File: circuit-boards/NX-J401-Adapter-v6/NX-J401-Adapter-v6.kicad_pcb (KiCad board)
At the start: 2 copper layers, 120 x 79 mm, 146 parts, among them J1 NX BUTTON, J10 SWD, J11 CFG, J12 NX CONTROL & UART, J13 NX BUTTON, J14 USB_C_Receptacle_USB2.0_14P, J2 POWER, J3 USB1, J4 USB2, J5 CAN1, J6 CAN1, J7 15V, J8 SWD, J9 CFG, Q1 SQM120P06-07L_GE3, Q10 SS8050, Q11 SI2301CDS-T1-GE3, Q2 CSD19534Q5A, Q3 CSD19534Q5A, Q4 CSD17578Q5A, Q5 CSD17578Q5A, Q6 SI2301CDS-T1-GE3, Q7 SS8050, Q8 SI2301CDS-T1-GE3, Q9 SI2301CDS-T1-GE3, SW1 RECOVERY, SW2 RESET, U2 RT9013-33GB, U3 STM32G431CBTx, U4 TJA1051TK-3, U5 RT9013-33GB, U6 STM32G431CBTx, U7 TJA1051TK-3, U8 FT232RNL, U9 ISO6721BDR

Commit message: Changed canable to use 3.3V power form USB to use key-e connector that breaks out USB and 3V3
Signed-off-by: Scott Berman <sgberman1@gmail.com>
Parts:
- removed C35, C39, C50: 1uF-50V-10%-0603, Capacitor_SMD:C_0603_1608Metric
- removed C49, C51, C52, C53, C55, C56: 0.1uF-50V-10%-0603, Capacitor_SMD:C_0603_1608Metric
- removed C54: 22uF-10%-16V-0805, Capacitor_SMD:C_0805_2012Metric
- removed D1: PC, LED_THT:LED_D3.0mm_Horizontal_O1.27mm_Z2.0mm
- removed J10: SWD, Connector_PinHeader_2.54mm:PinHeader_1x04_P2.54mm_Vertical
- removed J11: CFG, Connector_PinHeader_2.54mm:PinHeader_2x02_P2.54mm_Vertical
- removed J4: USB2, NX-J401-Adapter:Molex-70555-0003
- removed J6: CAN1, NX-J401-Adapter:Molex-70555-0001
- removed Q10: SS8050, Package_TO_SOT_SMD:SOT-23
- removed Q11, Q9: SI2301CDS-T1-GE3, Package_TO_SOT_SMD:SOT-23
- removed R26: 13K-1%-0603, Resistor_SMD:R_0603_1608Metric
- removed R27: 1M-1%-0603, Resistor_SMD:R_0603_1608Metric
- removed R28: 93.1k-1%-0603, Resistor_SMD:R_0603_1608Metric
- removed R29: 120R-1%-1206, Resistor_SMD:R_1206_3216Metric
- removed U2: RT9013-33GB, Package_TO_SOT_SMD:SOT-23-5
- removed U6: STM32G431CBTx, Package_QFP:LQFP-48_7x7mm_P0.5mm
- removed U7: TJA1051TK-3, Package_SON:HVSON-8-1EP_3x3mm_P0.65mm_EP1.6x2.4mm
- added D10: PC, LED_SMD:LED_1206_3216Metric, F.Cu at (69.3, 137.5)
- added D11: STAT, LED_SMD:LED_1206_3216Metric, F.Cu at (39.1, 135.9)
- added D9: PWR, LED_SMD:LED_1206_3216Metric, F.Cu at (69.3, 134.1)
- added L3: 2.2uH-41mOhm-20%, NX-J401-Adapter:KOHER-MDA4020-2R2M, F.Cu at (45.3, 133.5)
- added LP1: ~, NX-J401-Adapter:Bivar-LP-230, F.Cu at (249.8, 151.2)
- added LP3: ~, NX-J401-Adapter:Bivar-LP-230, F.Cu at (223.7, 151.4)
- C46: value 1uF-50V-10%-0603 -> 22uF-10%-16V-0805; footprint Capacitor_SMD:C_0603_1608Metric -> Capacitor_SMD:C_0805_2012Metric
- C47, C48: value 0.1uF-50V-10%-0603 -> 22uF-10%-16V-0805; footprint Capacitor_SMD:C_0603_1608Metric -> Capacitor_SMD:C_0805_2012Metric
- D8: value PESD1CAN -> WORD; footprint Package_TO_SOT_SMD:SOT-23 -> LED_SMD:LED_1206_3216Metric
- R18: value 93.1k-1%-0603 -> 2K-1%-0603
- R24: value 93.1k-1%-0603 -> 1K-1%-0603
- R25: value 13K-1%-0603 -> 1K-1%-0603
- U5: value RT9013-33GB -> TPS613222ADBV
- moved J3 191.8 mm to (241.0, 97.3), turned to 180 degrees
- moved J7 135.1 mm to (200.0, 88.5), turned to 90 degrees
- moved J1 127.1 mm to (176.5, 103.0)
- moved D8 59.0 mm to (39.1, 132.5)
- moved R25 50.1 mm to (29.4, 120.3)
- moved R24 50.1 mm to (29.4, 117.8)
- moved U4 49.3 mm to (22.4, 137.7)
- moved U5 48.5 mm to (46.0, 126.1)
- moved D2 44.3 mm to (71.9, 128.6)
- moved R23 42.3 mm to (27.8, 137.0)
- moved Q1 42.0 mm to (61.3, 118.1)
- moved C41 38.9 mm to (21.3, 122.8)
- moved R20 38.9 mm to (25.4, 122.8)
- moved C48 37.2 mm to (43.1, 122.0)
- moved C47 36.9 mm to (43.1, 119.0)
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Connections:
- net /CANable2.0-1/3V3_CAN renamed /CANable2.0/3V3_CAN
- net /CANable2.0-1/BOOT0 renamed /CANable2.0/BOOT0
- net /CANable2.0-1/CAN_H renamed /CANable2.0/CAN_H
- net /CANable2.0-1/CAN_L renamed /CANable2.0/CAN_L
- net /CANable2.0-1/CAN_TX renamed /CANable2.0/CAN_TX
- net /CANable2.0-1/NRST renamed /CANable2.0/NRST
- net /CANable2.0-1/SWCLK renamed /CANable2.0/SWCLK
- net /CANable2.0-1/SWDIO renamed /CANable2.0/SWDIO
- net /CANable2.0-1/USB_DM renamed /CANable2.0/USB_DM
- net /CANable2.0-1/USB_DP renamed /CANable2.0/USB_DP
- C37 pad 1: /CANable2.0-1/3V3 -> /CANable2.0/3V3
- C37 pad 2: /CANable2.0-1/GND_CAN -> /CANable2.0/GND_CAN
- C38 pad 1: /CANable2.0-1/3V3 -> /CANable2.0/3V3
- C38 pad 2: /CANable2.0-1/GND_CAN -> /CANable2.0/GND_CAN
- C40 pad 1: /CANable2.0-1/3V3 -> /CANable2.0/3V3
- C40 pad 2: /CANable2.0-1/GND_CAN -> /CANable2.0/GND_CAN
- C41 pad 1: /CANable2.0-1/3V3 -> /CANable2.0/3V3
- C41 pad 2: /CANable2.0-1/GND_CAN -> /CANable2.0/GND_CAN
- C42 pad 2: /CANable2.0-1/GND_CAN -> /CANable2.0/GND_CAN
- C43 pad 2: /CANable2.0-1/GND_CAN -> /CANable2.0/GND_CAN
- C44 pad 2: /CANable2.0-1/GND_CAN -> /CANable2.0/GND_CAN
- C45 pad 1: /CANable2.0-1/5V_CAN -> /CANable2.0/5V_CAN
- C45 pad 2: /CANable2.0-1/GND_CAN -> /CANable2.0/GND_CAN
- C46 pad 1: /CANable2.0-2/5V_CAN -> /CANable2.0/5V_CAN
- C46 pad 2: /CANable2.0-2/GND_CAN -> /CANable2.0/GND_CAN
- C47 pad 1: unconnected-(C47-Pad1) -> /CANable2.0/5V_CAN
- C47 pad 2: unconnected-(C47-Pad2) -> /CANable2.0/GND_CAN
- C48 pad 1: /CANable2.0-2/3V3 -> /CANable2.0/3V3
- C48 pad 2: /CANable2.0-2/GND_CAN -> /CANable2.0/GND_CAN
- D7 pad 3: /CANable2.0-1/GND_CAN -> /CANable2.0/GND_CAN
- D8 pad 1: /CANable2.0-2/CAN_L -> /CANable2.0/WORD_LED
- D8 pad 2: /CANable2.0-2/CAN_H -> Net-(D8-A)
- J3 pad 1: /CANable2.0-1/GND_CAN -> /CANable2.0/GND_CAN
- J3 pad 2: /CANable2.0-1/5V -> /CANable2.0/3V3
- J8 pad 1: /CANable2.0-1/3V3 -> /CANable2.0/3V3
- J8 pad 2: /CANable2.0-1/GND_CAN -> /CANable2.0/GND_CAN
- J9 pad 3: /CANable2.0-1/3V3 -> /CANable2.0/3V3
- Q6 pad 1: /CANable2.0-1/GND_CAN -> /CANable2.0/GND_CAN
- Q6 pad 2: /CANable2.0-1/5V_CAN -> /CANable2.0/3V3
- Q6 pad 3: /CANable2.0-1/5V -> /CANable2.0/3V3
- Q7 pad 2: /CANable2.0-1/GND_CAN -> /CANable2.0/GND_CAN
- Q8 pad 2: /CANable2.0-1/3V3 -> /CANable2.0/3V3
- R18 pad 1: /CANable2.0-1/5V_CAN -> /15V 3A Buck-Boost Power Supply/+V_IN
- R18 pad 2: /CANable2.0-1/GND_CAN -> Net-(D9-A)
- R19 pad 2: /CANable2.0-1/GND_CAN -> /CANable2.0/GND_CAN
- R20 pad 1: /CANable2.0-1/3V3 -> /CANable2.0/3V3
- R21 pad 1: /CANable2.0-1/3V3 -> /CANable2.0/3V3
- R22 pad 1: /CANable2.0-1/3V3 -> /CANable2.0/3V3
- R24 pad 1: /CANable2.0-2/5V_CAN -> /CANable2.0/3V3
- R24 pad 2: /CANable2.0-2/GND_CAN -> Net-(D8-A)
- R25 pad 1: /CANable2.0-2/BOOT0 -> /CANable2.0/3V3
- R25 pad 2: /CANable2.0-2/GND_CAN -> Net-(D11-A)
- U3 pad 1: /CANable2.0-1/3V3 -> /CANable2.0/3V3
- U3 pad 19: /CANable2.0-1/GND_CAN -> /CANable2.0/GND_CAN
- U3 pad 20: /CANable2.0-1/3V3 -> /CANable2.0/3V3
- U3 pad 21: /CANable2.0-1/3V3 -> /CANable2.0/3V3
- U3 pad 23: /CANable2.0-1/GND_CAN -> /CANable2.0/GND_CAN
- U3 pad 24: /CANable2.0-1/3V3 -> /CANable2.0/3V3
- U3 pad 35: /CANable2.0-1/GND_CAN -> /CANable2.0/GND_CAN
- U3 pad 36: /CANable2.0-1/3V3 -> /CANable2.0/3V3
- U3 pad 39: /CANable2.0-1/STAT_LED -> /CANable2.0/STAT_LED
- U3 pad 47: /CANable2.0-1/GND_CAN -> /CANable2.0/GND_CAN
- U3 pad 48: /CANable2.0-1/3V3 -> /CANable2.0/3V3
- U3 pad 8: /CANable2.0-1/WORD_LED -> /CANable2.0/WORD_LED
- U4 pad 2: /CANable2.0-1/GND_CAN -> /CANable2.0/GND_CAN
- U4 pad 3: /CANable2.0-1/5V_CAN -> /CANable2.0/5V_CAN
- U4 pad 8: /CANable2.0-1/GND_CAN -> /CANable2.0/GND_CAN
- U4 pad 9: /CANable2.0-1/GND_CAN -> /CANable2.0/GND_CAN
- U5 pad 1: /CANable2.0-2/5V_CAN -> Net-(U5-SW)
- U5 pad 2: /CANable2.0-2/GND_CAN -> /CANable2.0/GND_CAN
- U5 pad 3: /CANable2.0-2/5V_CAN -> unconnected-(U5-NC-Pad3)
- U5 pad 4: unconnected-(U5-NC-Pad4) -> /CANable2.0/5V_CAN
- U5 pad 5: /CANable2.0-2/3V3 -> unconnected-(U5-NC-Pad5)

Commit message: WIP update
Signed-off-by: Scott Berman <sgberman1@gmail.com>
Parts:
- removed J1: NX BUTTON, NX-J401-Adapter:Molex-0878331031
- added J10: NX CONTROL & UART, Connector_PinHeader_2.54mm:PinHeader_1x18_P2.54mm_Horizontal, F.Cu at (193.7, 85.0)
- added J4: Terminal, NX-J401-Adapter:Keystone-7774, F.Cu at (186.2, 74.5)
- added J6: Terminal, NX-J401-Adapter:Keystone-7774, F.Cu at (244.3, 74.5)
- J13: value NX BUTTON -> NX CONTROL & UART; footprint NX-J401-Adapter:Molex-878321010 -> Connector_PinSocket_2.54mm:PinSocket_1x18_P2.54mm_Vertical
- J8: footprint Connector_PinHeader_2.54mm:PinHeader_1x04_P2.54mm_Vertical -> Connector_PinHeader_2.54mm:PinHeader_1x04_P2.54mm_Horizontal
- J9: footprint Connector_PinHeader_2.54mm:PinHeader_2x02_P2.54mm_Vertical -> Connector_PinHeader_2.54mm:PinHeader_1x04_P2.54mm_Horizontal
- moved J8 206.9 mm to (245.4, 108.9)
- moved J9 206.9 mm to (245.4, 121.1)
- moved J13 113.1 mm to (122.9, 82.3)
- moved J5 61.4 mm to (178.0, 140.5)
- moved J14 57.5 mm to (247.0, 148.6)
- moved LP1 52.4 mm to (197.4, 151.4)
- moved SW1 52.4 mm to (225.1, 150.6)
- moved SW2 52.1 mm to (214.1, 150.6)
- moved J2 48.5 mm to (165.9, 144.1)
- moved J7 33.9 mm to (170.5, 105.2), turned to 0 degrees
- moved LP3 32.7 mm to (190.9, 151.4)
- moved J3 8.49 mm to (245.1, 89.9), turned to 0 degrees
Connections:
- J13 pad 1: /NX-Button Interface/NX_PC_LED- -> /NX-Button Interface/CAN_TX
- J13 pad 10: /NX-Button Interface/GND_BTN -> /NX-Button Interface/UART2_TXD
- J13 pad 2: /NX-Button Interface/NX_PC_LED+ -> /NX-Button Interface/CAN_RX
- J13 pad 3: /NX-Button Interface/~{REC} -> /NX-Button Interface/GND_BTN
- J13 pad 4: /NX-Button Interface/GND_BTN -> /NX-Button Interface/3V3_BTN
- J13 pad 5: /NX-Button Interface/~{SYS_RESET} -> unconnected-(J13-Pin_5-Pad5)
- J13 pad 6: /NX-Button Interface/UART2_RXD -> unconnected-(J13-Pin_6-Pad6)
- J13 pad 7: /NX-Button Interface/GND_BTN -> /NX-Button Interface/NX_PC_LED-
- J13 pad 8: /NX-Button Interface/UART2_TXD -> /NX-Button Interface/NX_PC_LED+
- J13 pad 9: /NX-Button Interface/3V3_BTN -> /NX-Button Interface/UART2_RXD
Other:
- outline, holes or cut-outs redrawn

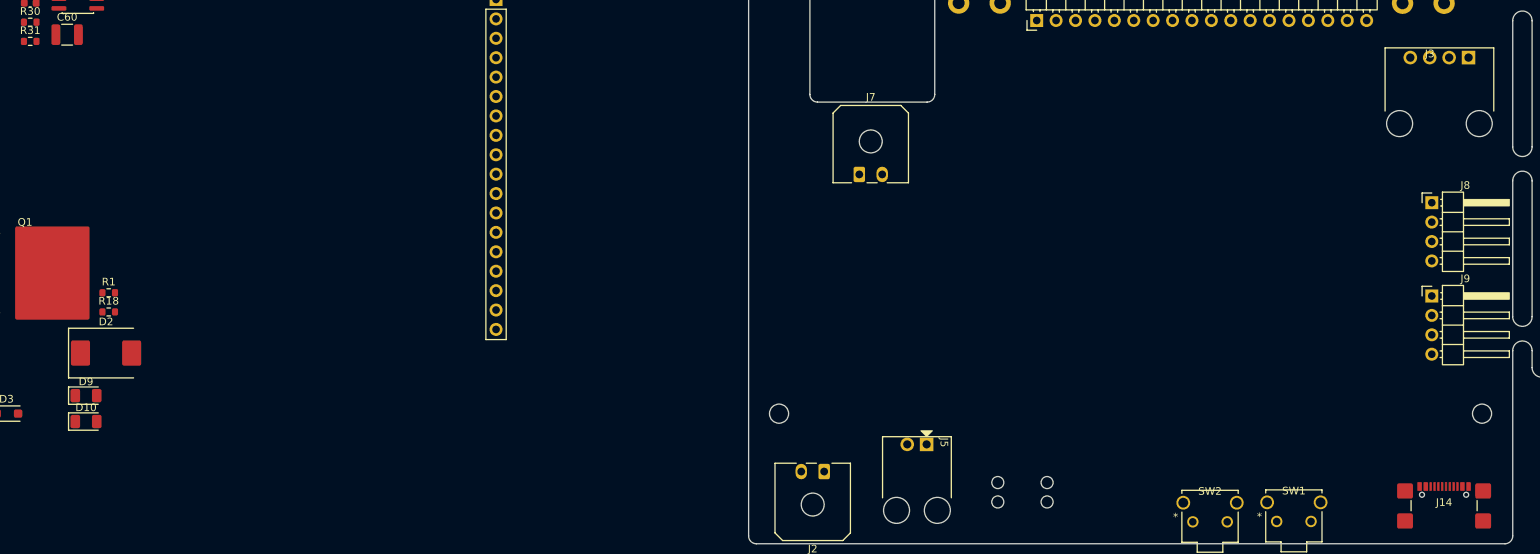
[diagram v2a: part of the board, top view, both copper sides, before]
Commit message: Changed USB header ot pico lock and light pipe to single row
Signed-off-by: Scott Berman <sgberman1@gmail.com>
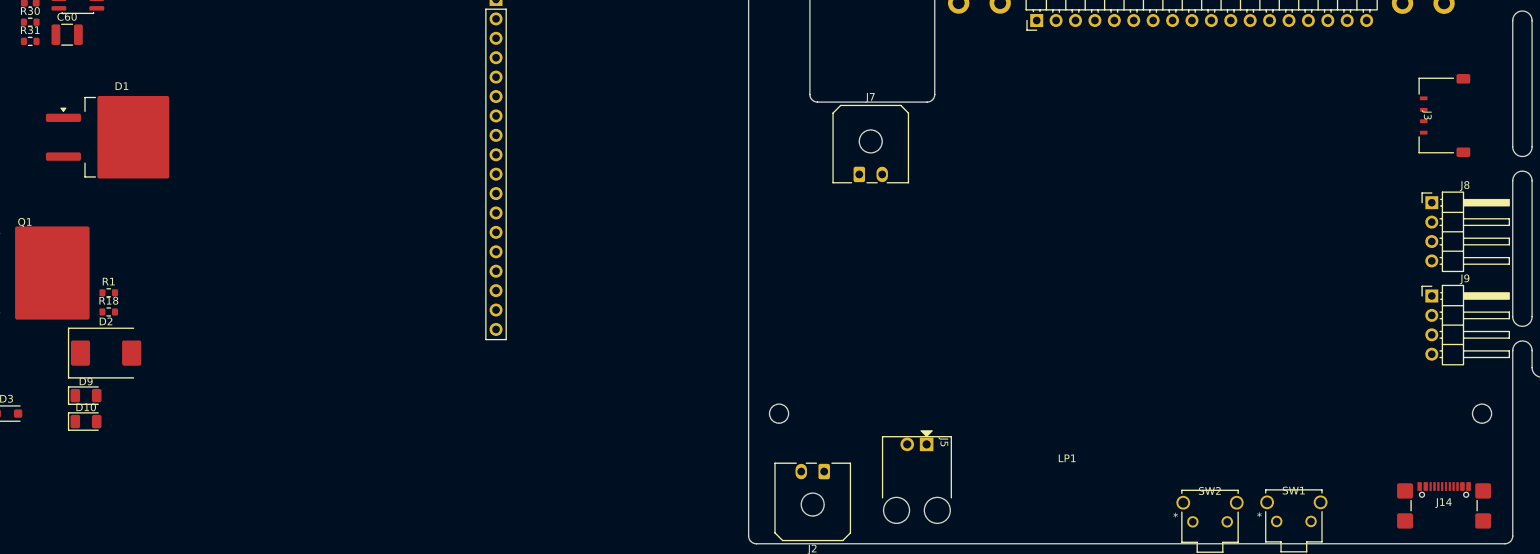
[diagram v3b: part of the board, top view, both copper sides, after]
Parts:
- removed LP3: ~, NX-J401-Adapter:Bivar-LP-230
- added D1: STPS20M100SG-TR, Package_TO_SOT_SMD:TO-263-2, F.Cu at (74.0, 100.3)
- J3: footprint NX-J401-Adapter:Molex-70555-0003 -> NX-J401-Adapter:Molex-PicoLatch-5040500491
- LP1: footprint NX-J401-Adapter:Bivar-LP-230 -> NX-J401-Adapter:Bivar-RLP4-200-500
- moved LP1 8.53 mm to (197.7, 142.9)
- moved J3 7.62 mm to (244.3, 97.5), turned to -90 degrees
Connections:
- C19 pad 1: /V_OUT -> /15V 3A Buck-Boost Power Supply/+V_OUT
- C23 pad 1: /V_OUT -> /15V 3A Buck-Boost Power Supply/+V_OUT
- C24 pad 1: /V_OUT -> /15V 3A Buck-Boost Power Supply/+V_OUT
- C25 pad 1: /V_OUT -> /15V 3A Buck-Boost Power Supply/+V_OUT
- C26 pad 1: /V_OUT -> /15V 3A Buck-Boost Power Supply/+V_OUT
- C27 pad 1: /V_OUT -> /15V 3A Buck-Boost Power Supply/+V_OUT
- C28 pad 1: /V_OUT -> /15V 3A Buck-Boost Power Supply/+V_OUT
- C29 pad 1: /V_OUT -> /15V 3A Buck-Boost Power Supply/+V_OUT
- C30 pad 1: /V_OUT -> /15V 3A Buck-Boost Power Supply/+V_OUT
- C31 pad 1: /V_OUT -> /15V 3A Buck-Boost Power Supply/+V_OUT
- C32 pad 1: /V_OUT -> /15V 3A Buck-Boost Power Supply/+V_OUT
- C33 pad 1: /V_OUT -> /15V 3A Buck-Boost Power Supply/+V_OUT
- C34 pad 1: /V_OUT -> /15V 3A Buck-Boost Power Supply/+V_OUT
- Q4 pad 5: /V_OUT -> /15V 3A Buck-Boost Power Supply/+V_OUT
- R16 pad 1: /V_OUT -> /15V 3A Buck-Boost Power Supply/+V_OUT
- U1 pad 24: /V_OUT -> /15V 3A Buck-Boost Power Supply/+V_OUT

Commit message: Added ideal diode circuit for reverse polarity and output or-ing
Signed-off-by: Scott Berman <sgberman1@gmail.com>
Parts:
- removed D1: STPS20M100SG-TR, Package_TO_SOT_SMD:TO-263-2
- removed D3: 15V, Diode_SMD:D_SOD-123F
- removed Q1: SQM120P06-07L_GE3, NX-J401-Adapter:TO-263-2
- removed R1: 5.9k-1%-0603, Resistor_SMD:R_0603_1608Metric
- added C35: 0.1uF-50V-10%-0603, Capacitor_SMD:C_0603_1608Metric, F.Cu at (56.5, 133.6)
- added C39: 0.1uF-50V-10%-0603, Capacitor_SMD:C_0603_1608Metric, F.Cu at (56.5, 136.1)
- added Q10: CSD19534Q5A, NX-J401-Adapter:TI-SON5x6, F.Cu at (50.9, 141.7)
- added Q9: CSD19534Q5A, NX-J401-Adapter:TI-SON5x6, F.Cu at (50.9, 135.4)
- added U2: LM74700QDBVRQ1, Package_TO_SOT_SMD:SOT-23-6, F.Cu at (60.7, 147.4)
- added U6: LM74700QDBVRQ1, Package_TO_SOT_SMD:SOT-23-6, F.Cu at (60.7, 152.1)
- moved J13 74.5 mm to (48.5, 84.8)
- moved C6 73.6 mm to (44.4, 138.7)
- moved U4 71.5 mm to (93.2, 127.8)
- moved C59 70.2 mm to (99.9, 131.8)
- moved C63 70.2 mm to (99.9, 139.3)
- moved C64 70.2 mm to (99.9, 141.8)
- moved L2 70.2 mm to (112.6, 138.7)
- moved R31 70.2 mm to (99.9, 146.9)
- moved U8 70.2 mm to (107.1, 131.4)
- moved C57 70.2 mm to (99.9, 126.8)
- moved C58 70.2 mm to (99.9, 129.3)
- moved C60 70.2 mm to (104.7, 146.0)
- moved C61 70.2 mm to (99.9, 134.3)
- moved C62 70.2 mm to (99.9, 136.8)
- moved R30 70.2 mm to (99.9, 144.4)
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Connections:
- C34 pad 1: /15V 3A Buck-Boost Power Supply/+V_OUT -> /V_OUT
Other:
- copper layers 2 -> 4

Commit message: Starting component placement
Signed-off-by: Scott Berman <sgberman1@gmail.com>
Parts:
- C10, C12, C15, C17, C18, C28, C29, C30, C31, C32, C35, C39: moved to B.Cu
- moved C33 162.5 mm to (201.2, 100.3)
- moved C34 150.7 mm to (185.9, 95.2), turned to -90 degrees
- moved Q10 148.0 mm to (191.0, 94.2), turned to -90 degrees
- moved U6 146.3 mm to (196.2, 96.9), turned to 180 degrees
- moved C39 146.2 mm to (197.4, 96.9), turned to -90 degrees
- moved D9 129.2 mm to (190.1, 144.5), turned to 90 degrees
- moved C27 124.7 mm to (201.2, 96.8)
- moved C6 124.5 mm to (168.1, 124.7)
- moved C23 124.4 mm to (201.2, 103.9)
- moved C24 124.4 mm to (201.2, 107.4)
- moved C25 124.2 mm to (201.2, 110.9)
- moved C1 123.7 mm to (168.1, 131.6)
- moved C26 121.8 mm to (198.8, 114.9), turned to -90 degrees
- moved C28 119.3 mm to (201.2, 100.3)
- moved C29 119.2 mm to (201.2, 103.9)
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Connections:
- net /15V 3A Buck-Boost Power Supply/+V_IN renamed /VIN_PS
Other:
- outline, holes or cut-outs redrawn

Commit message: rearrange power supply
Signed-off-by: Scott Berman <scott.berman@bluerivertech.com>
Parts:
- moved C27 24.3 mm to (190.5, 118.6), turned to -90 degrees
- moved C28 16.6 mm to (190.5, 113.0), turned to 90 degrees
- moved C33 16.6 mm to (190.5, 113.0), turned to 90 degrees
- moved C23 15.1 mm to (197.6, 118.6), turned to -90 degrees
- moved C29 15.1 mm to (197.6, 118.6), turned to -90 degrees
- moved Q10 13.9 mm to (194.1, 107.7), turned to 0 degrees
- moved C24 13.2 mm to (194.1, 118.6), turned to -90 degrees
- moved C30 13.2 mm to (194.1, 118.6), turned to -90 degrees
- moved C34 12.7 mm to (188.4, 107.7)
- moved C17 10.3 mm to (164.8, 120.4)
- moved C18 10.3 mm to (161.2, 120.4)
- moved C7 10.3 mm to (164.8, 120.4)
- moved C8 10.3 mm to (161.2, 120.4)
- moved Q2 8.31 mm to (169.5, 115.4)
- moved R15 8.31 mm to (177.7, 119.9)
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
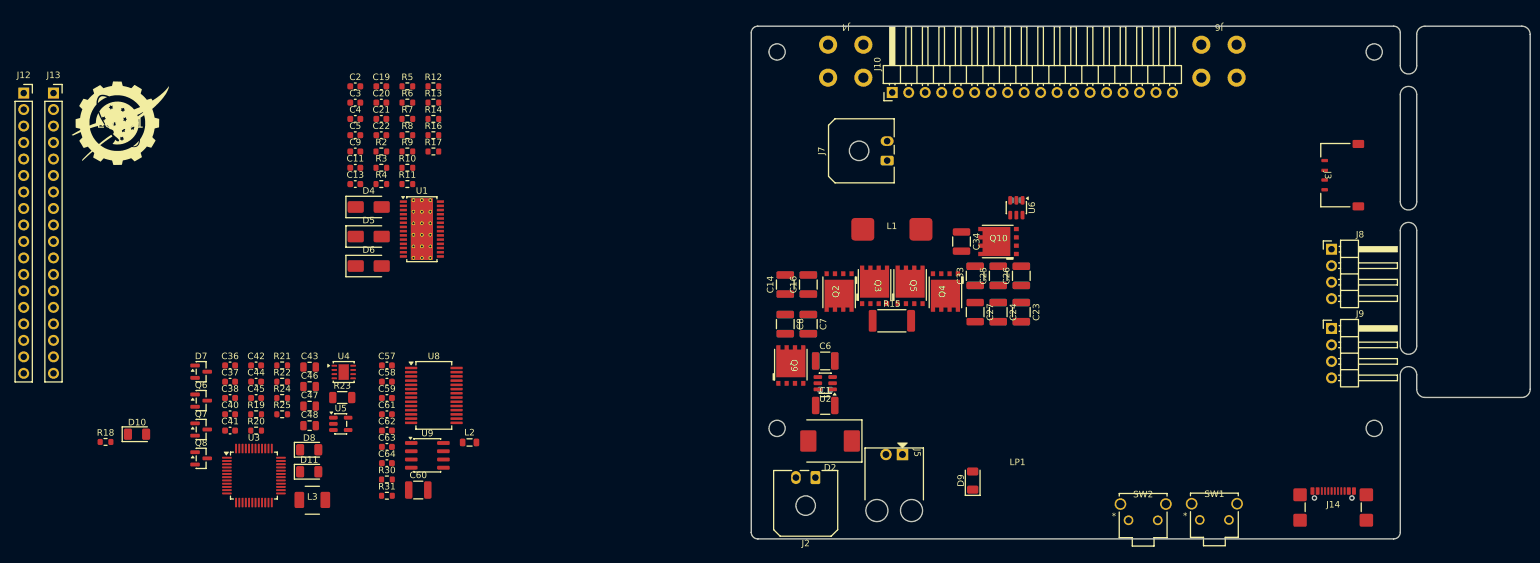
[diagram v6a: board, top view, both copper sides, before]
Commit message: Improved placement.  Pre-routing
Signed-off-by: Scott Berman <sgberman1@gmail.com>
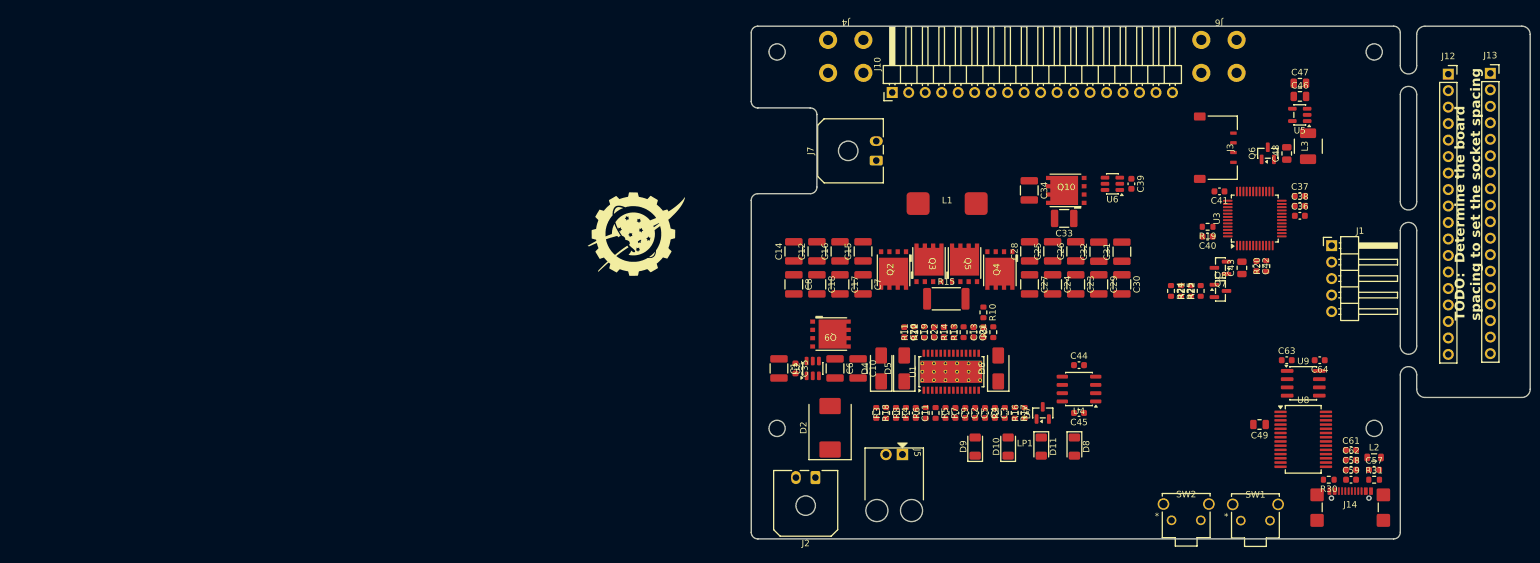
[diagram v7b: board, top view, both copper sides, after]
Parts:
- removed C60: 10uF-50V-10%-X7R-1210, Capacitor_SMD:C_1210_3225Metric
- removed J8: SWD, Connector_PinHeader_2.54mm:PinHeader_1x04_P2.54mm_Horizontal
- removed J9: CFG, Connector_PinHeader_2.54mm:PinHeader_1x04_P2.54mm_Horizontal
- removed R23: 120R-1%-1206, Resistor_SMD:R_1206_3216Metric
- added C49: 22uF-10%-16V-0805, Capacitor_SMD:C_0805_2012Metric, F.Cu at (234.3, 135.9)
- added J1: SWD, Connector_PinHeader_2.54mm:PinHeader_1x05_P2.54mm_Horizontal, F.Cu at (245.4, 108.3)
- C10, C12, C15, C17, C18, C28, C29, C30, C31, C32, C35, C39: moved to F.Cu
- U4: value TJA1051TK-3 -> TJA1051T/3/1J; footprint Package_SON:HVSON-8-1EP_3x3mm_P0.65mm_EP1.6x2.4mm -> Package_SO:SO-8_3.9x4.9mm_P1.27mm
- moved J13 221.4 mm to (269.9, 81.8)
- moved J12 219.5 mm to (263.4, 81.9)
- moved Q6 168.7 mm to (235.6, 94.1), turned to 90 degrees
- moved C38 167.5 mm to (240.5, 102.2)
- moved C37 167.3 mm to (240.5, 100.7)
- moved C36 166.4 mm to (240.5, 103.7)
- moved L3 162.8 mm to (241.8, 93.0), turned to 90 degrees
- moved C47 160.5 mm to (240.5, 83.3)
- moved U3 159.2 mm to (233.6, 104.2), turned to 90 degrees
- moved Q8 159.2 mm to (228.3, 115.3)
- moved Q7 159.0 mm to (228.3, 111.8), turned to 180 degrees
- moved C46 159.0 mm to (240.5, 85.3)
- moved R20 157.7 mm to (235.4, 111.5), turned to 90 degrees
- moved C41 156.8 mm to (228.1, 100.0), turned to 180 degrees
- moved C48 156.3 mm to (238.5, 94.1), turned to 90 degrees
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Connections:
- C36 pad 1: unconnected-(C36-Pad1) -> /CANable2.0/3V3
- C36 pad 2: unconnected-(C36-Pad2) -> /CANable2.0/GND_CAN
- J3 pad 2: /CANable2.0/3V3 -> /CANable2.0/3V3_USB
- Q6 pad 3: /CANable2.0/3V3 -> /CANable2.0/3V3_USB
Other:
- outline, holes or cut-outs redrawn
- board text added: "TODO: Determine the board spacing to set the socket spacing"
